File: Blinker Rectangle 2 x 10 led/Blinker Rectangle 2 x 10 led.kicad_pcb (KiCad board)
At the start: 2 copper layers, 65 x 40 mm, 46 parts, among them J1 To Base, J2 To Base

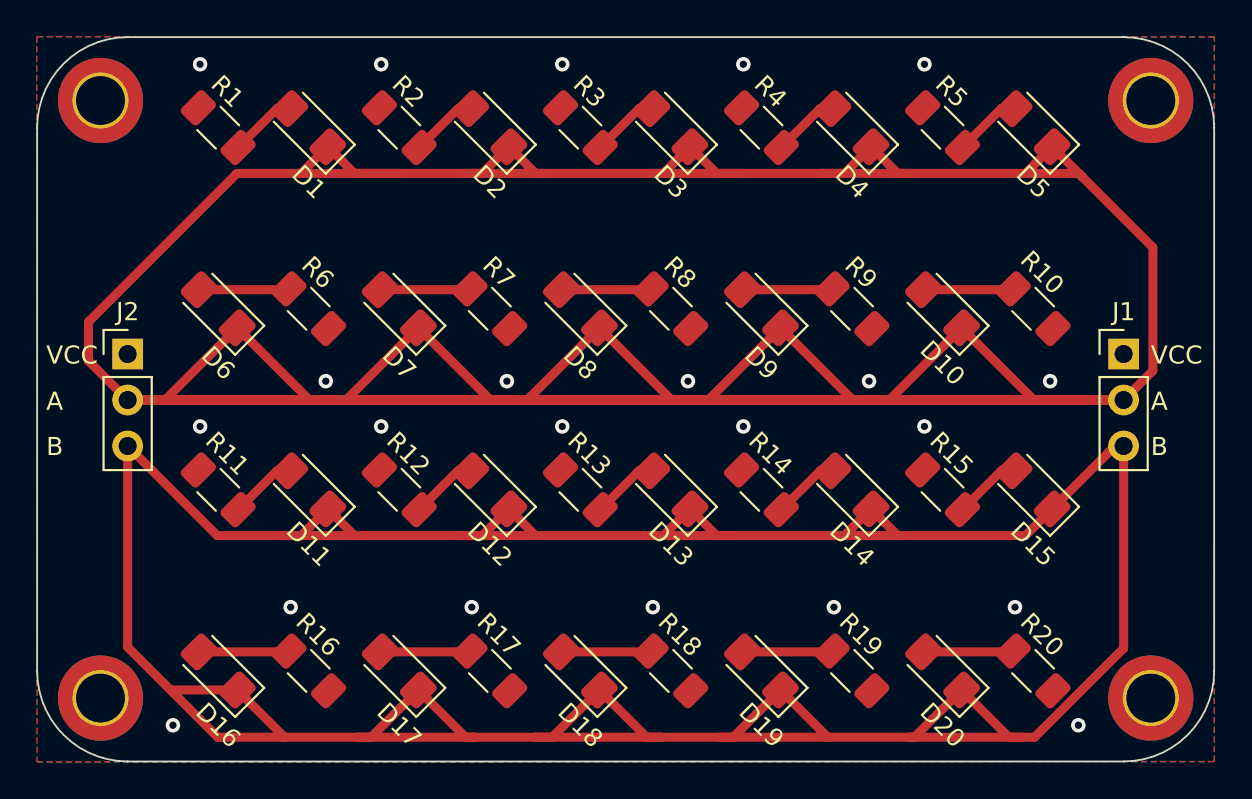
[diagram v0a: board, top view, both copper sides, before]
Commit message: Fix clearances
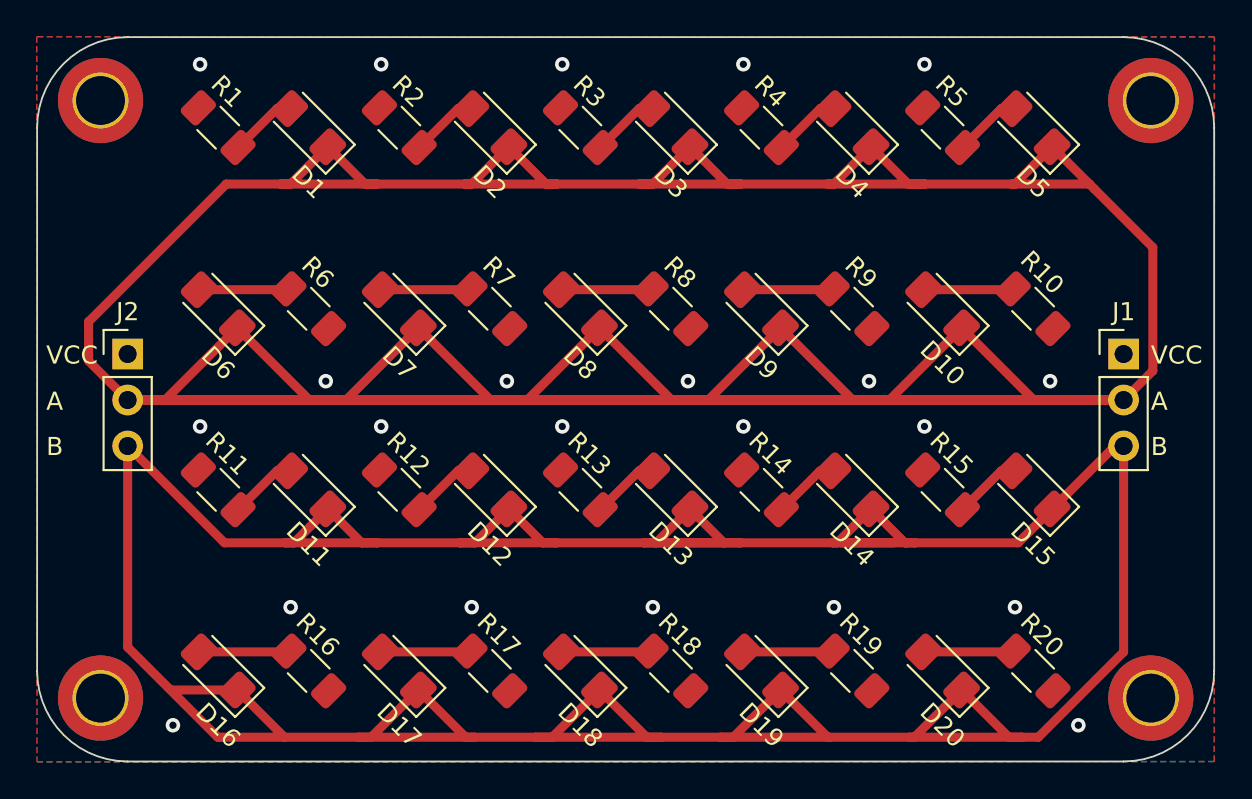
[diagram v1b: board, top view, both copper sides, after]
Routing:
- net Net-(D11-K): track 203.9 -> 215.8 mm
- net Net-(D1-K): track 399.5 -> 403.4 mm
